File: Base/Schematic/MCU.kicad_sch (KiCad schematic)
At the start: 6 parts, among them U1 STM32F446RET6, X1 1532H4-12000JWPDTSNL

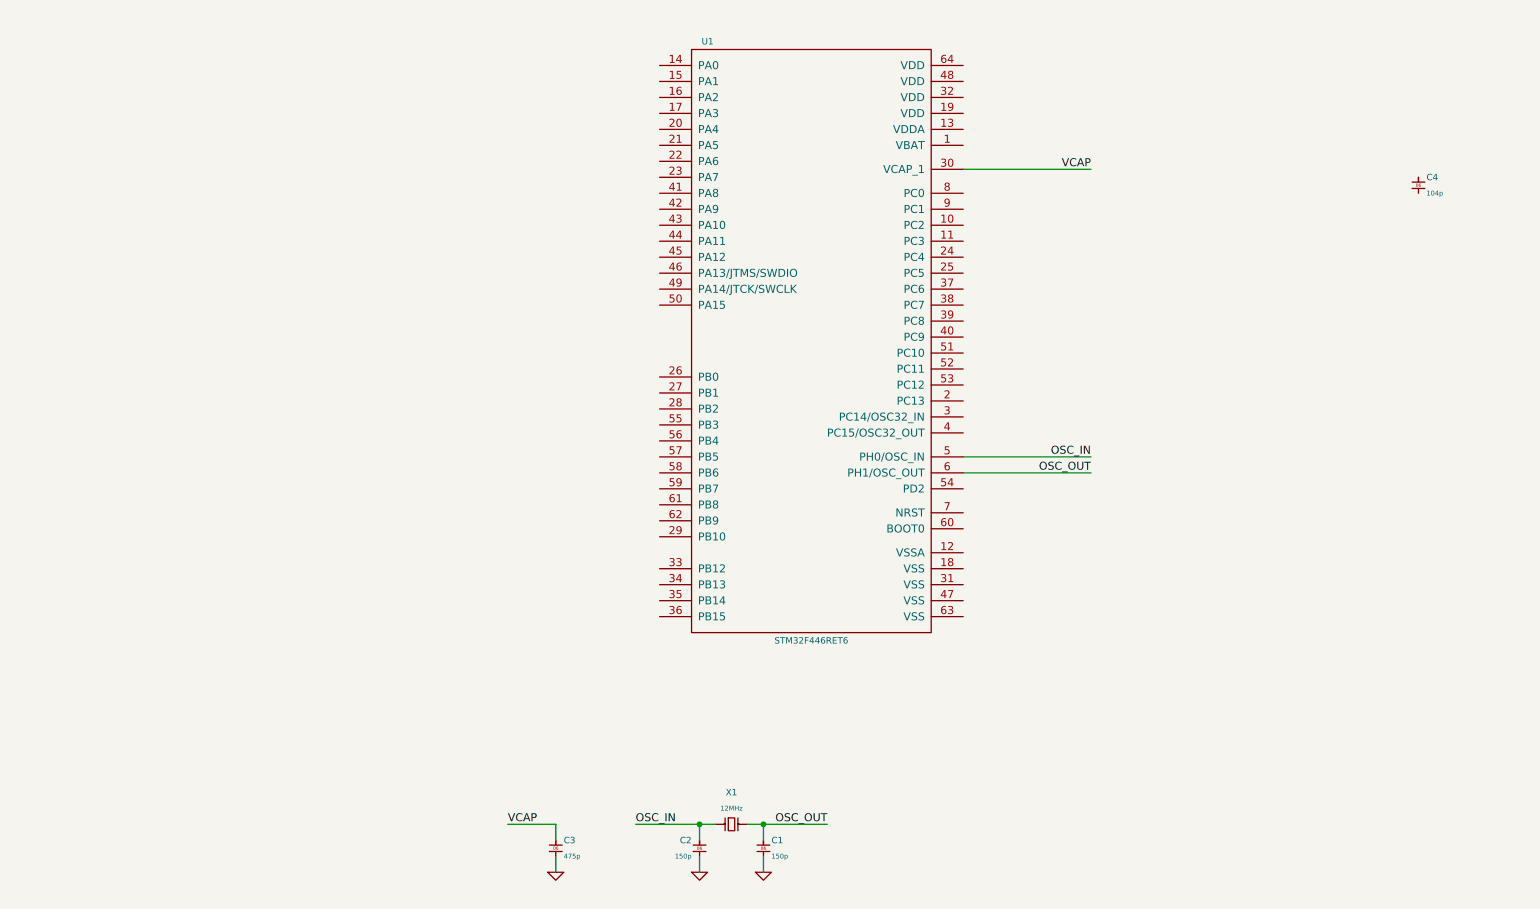
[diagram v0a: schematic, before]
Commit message: [Base 회로 업데이트] - 전원 회로 추가
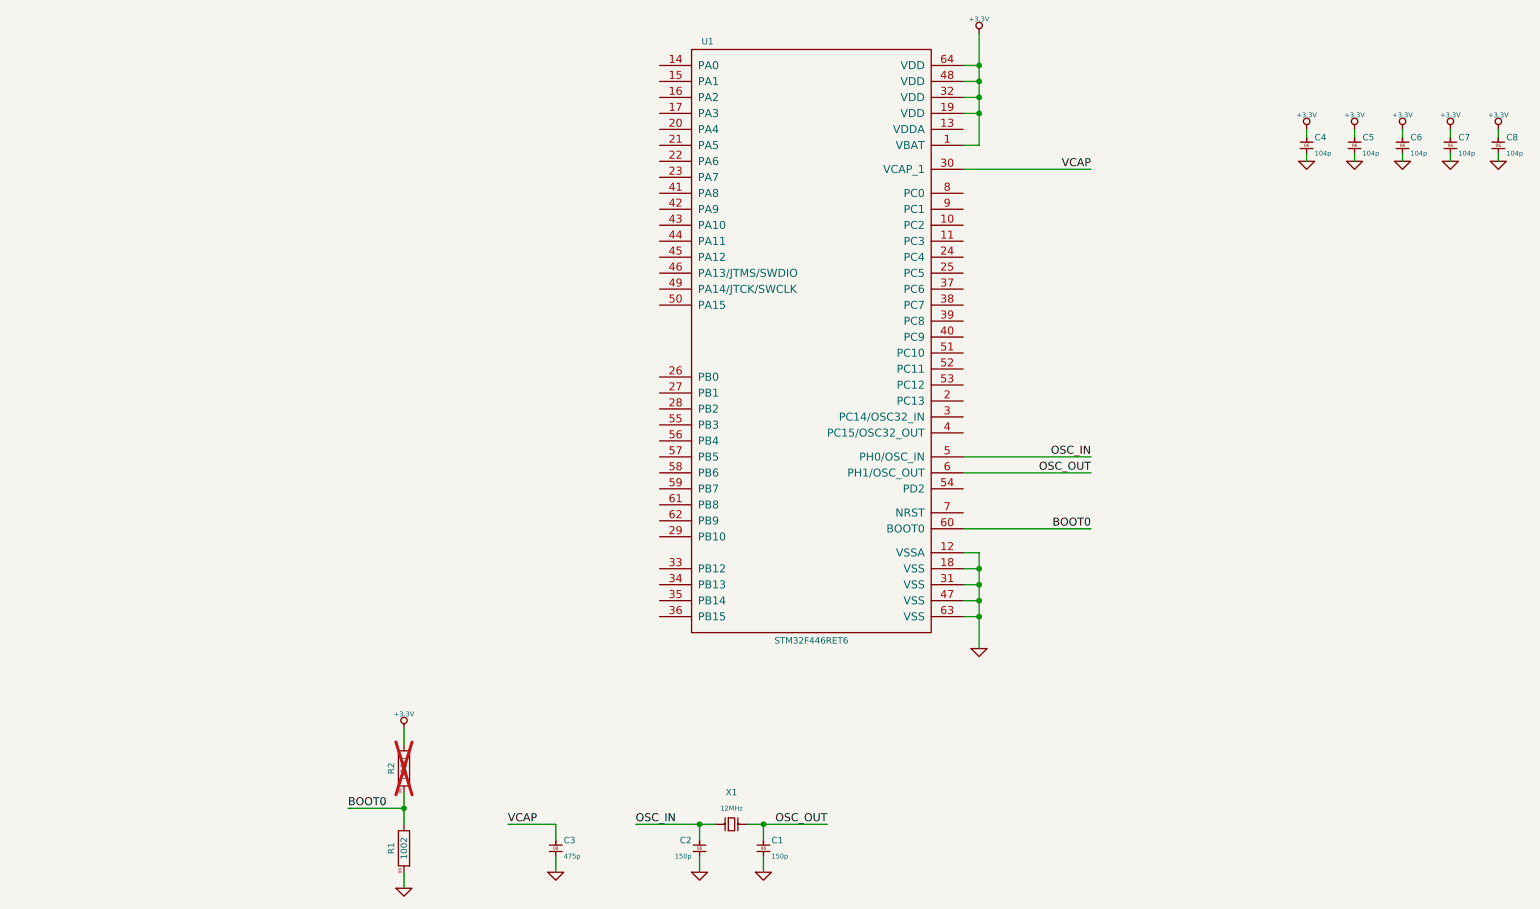
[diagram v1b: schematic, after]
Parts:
- added C5, C6, C7, C8: 0603B104K500, SMC:0603, symbol Capacitor_MLCC:0603B104K500
- added R1: WR06X1002FTL, SMR:0603, symbol Resistor:WR06X1002FTL
- added R2: WR06X0000JTL, SMR:0603, symbol Resistor:WR06X0000JTL
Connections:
- net GND: now also C4.1, U1.12 (VSSA), U1.18 (VSS), U1.31 (VSS), U1.47 (VSS), U1.63 (VSS), C5.1, C6.1, C7.1, C8.1, R1.1
- net +3.3V: now reaches U1.1 (VBAT)
- net +3.3V: now also C4.2, U1.19 (VDD), U1.32 (VDD), U1.48 (VDD), U1.64 (VDD), C5.2, C6.2, C7.2, C8.2, R2.2
- net BOOT0: now reaches U1.60 (BOOT0)
- net BOOT0: now also R1.2, R2.1
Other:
- moved on the sheet: C4

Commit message: [Base 회로도 업데이트] - MCU를 STM32F446 -> Nuvoton M433으로 변경
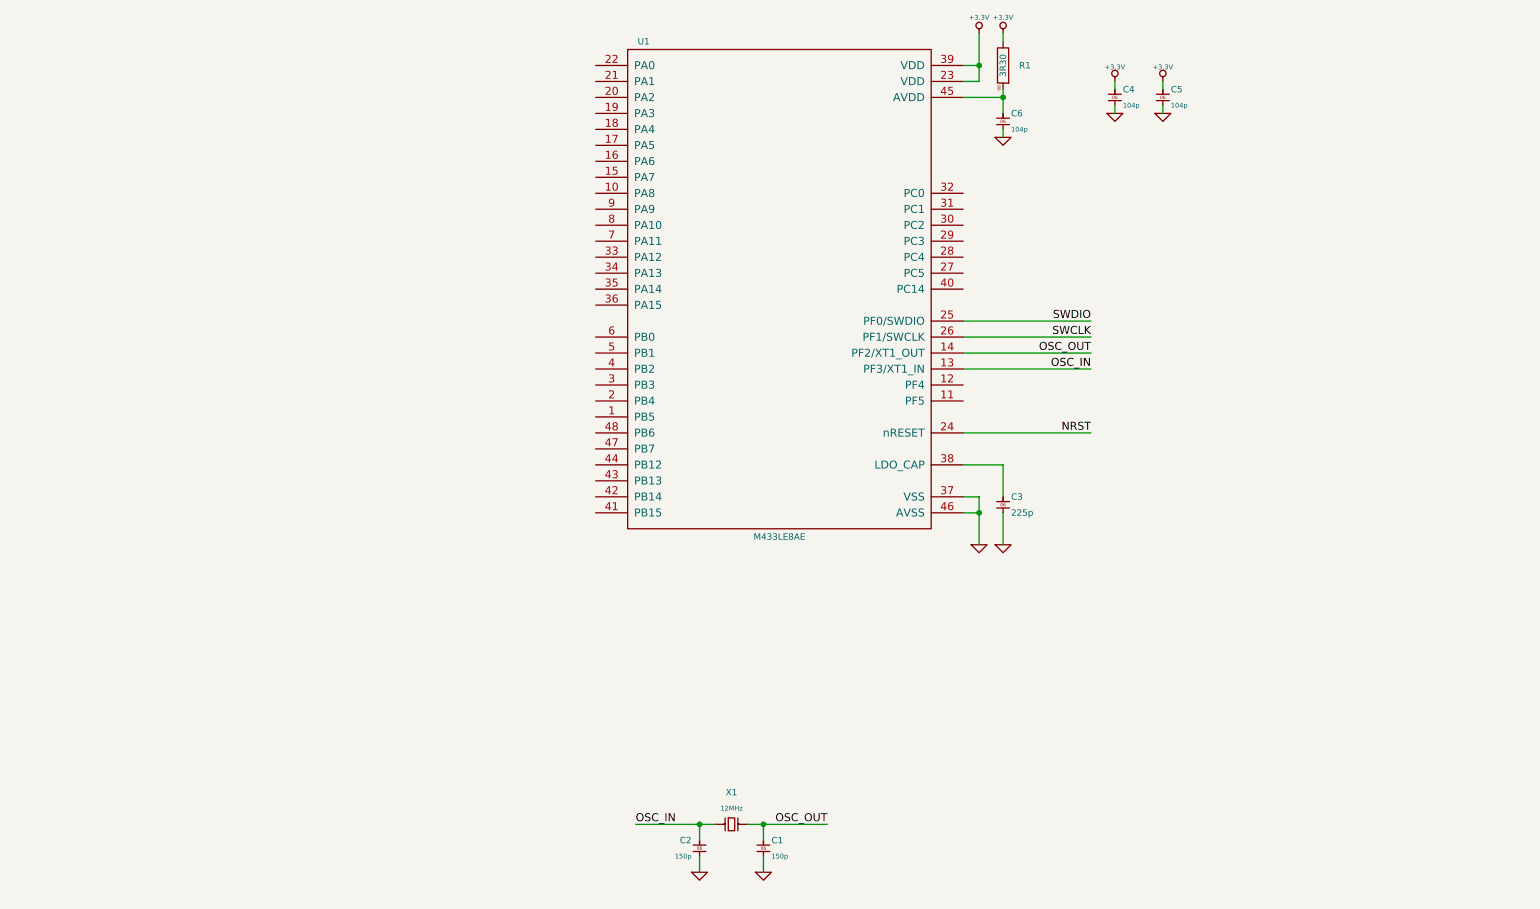
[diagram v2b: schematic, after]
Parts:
- removed C3: 0603X475K100, SMC:0603, symbol Capacitor_MLCC:0603X475K100
- removed C7, C8: 0603B104K500, SMC:0603, symbol Capacitor_MLCC:0603B104K500
- removed R1: WR06X1002FTL, SMR:0603, symbol Resistor:WR06X1002FTL
- removed R2: WR06X0000JTL, SMR:0603, symbol Resistor:WR06X0000JTL
- removed U1: STM32F446RET6, LQFP:LQFP64, symbol MCU:STM32F446RET6
- added C3: 0603X225K100, Capacitor_SMD:C_0603_1608Metric_Pad1.08x0.95mm_HandSolder, symbol Capacitor_MLCC:0603X225K100
- added R1: WR06W3R30FTL, SMR:0603, symbol Resistor:WR06W3R30FTL
- added U1: M433LE8AE, LQFP:LQFP48, symbol MCU:M433LE8AE
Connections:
- net +3.3V: now also R1.2, U1.23 (VDD), U1.39 (VDD); no longer C6.2
- net GND: now also C3.1, U1.37 (VSS), U1.46 (AVSS)
- net OSC_IN: now also U1.13 (PF3/XT1_IN)
- net OSC_OUT: now also U1.14 (PF2/XT1_OUT)
- new net: C6.2, R1.1, U1.45 (AVDD)
- new net: C3.2, U1.38 (LDO_CAP)
- new net NRST: U1.24 (nRESET)
- new net SWCLK: U1.26 (PF1/SWCLK)
- new net SWDIO: U1.25 (PF0/SWDIO)
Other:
- moved on the sheet: C4, C5

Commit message: [Base 회로도 업데이트] - RTC 회로 추가 - M433에는 VBAT 단자가 없어서 별도 부품으로 추가함
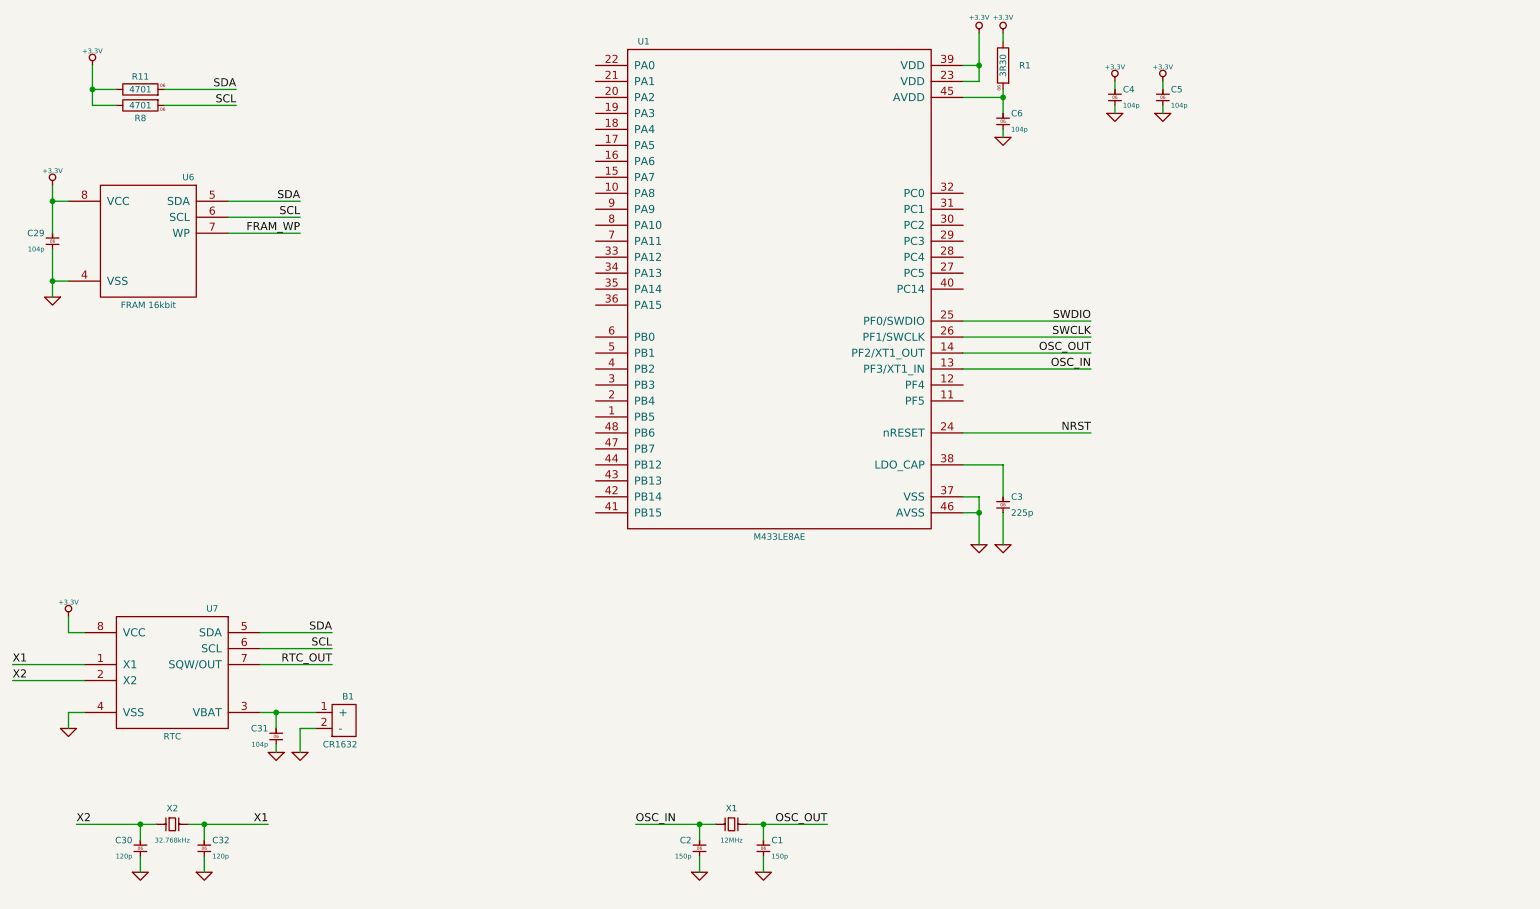
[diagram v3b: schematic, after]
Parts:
- added B1: GT-CR1632-1Au, G-Switch:GT-CR1632-1Au, symbol BatteryHolder:GT-CR1632-1Au
- added C29, C31: 0603B104K500, SMC:0603, symbol Capacitor_MLCC:0603B104K500
- added C30, C32: 0603N120J500, SMC:0603, symbol Capacitor_MLCC:0603N120J500
- added R11, R8: WR06X4701FTL, SMR:0603, symbol Resistor:WR06X4701FTL
- added U6: MB85RC16PNF-G-JNE, SO:SOIC-8, symbol FRAM:MB85RC16PNF-G-JNE
- added U7: SL1307ZN+T, SO:SOIC-8, symbol RTC:SL1307ZN+T
- added X2: XKXGI-SUA-32.768K, CRYSTAL:SMD_3215_2Pin, symbol Crystal:XKXGI-SUA-32.768K
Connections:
- net +3.3V: now also C29.2, R11.2, R8.2, U6.8 (VCC), U7.8 (VCC)
- net GND: now also B1.2 (-), C29.1, C30.1, C31.1, C32.1, U6.4 (VSS), U7.4 (VSS)
- new net: B1.1 (+), C31.2, U7.3 (VBAT)
- new net FRAM_WP: U6.7 (WP)
- new net RTC_OUT: U7.7 (SQW/OUT)
- new net SCL: R8.1, U6.6 (SCL), U7.6 (SCL)
- new net SDA: R11.1, U6.5 (SDA), U7.5 (SDA)
- new net X1: C32.2, U7.1 (X1), X2.2
- new net X2: C30.2, U7.2 (X2), X2.1

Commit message: [Base PCB 업데이트] - PCB 외곽선과 볼트 위치 설정
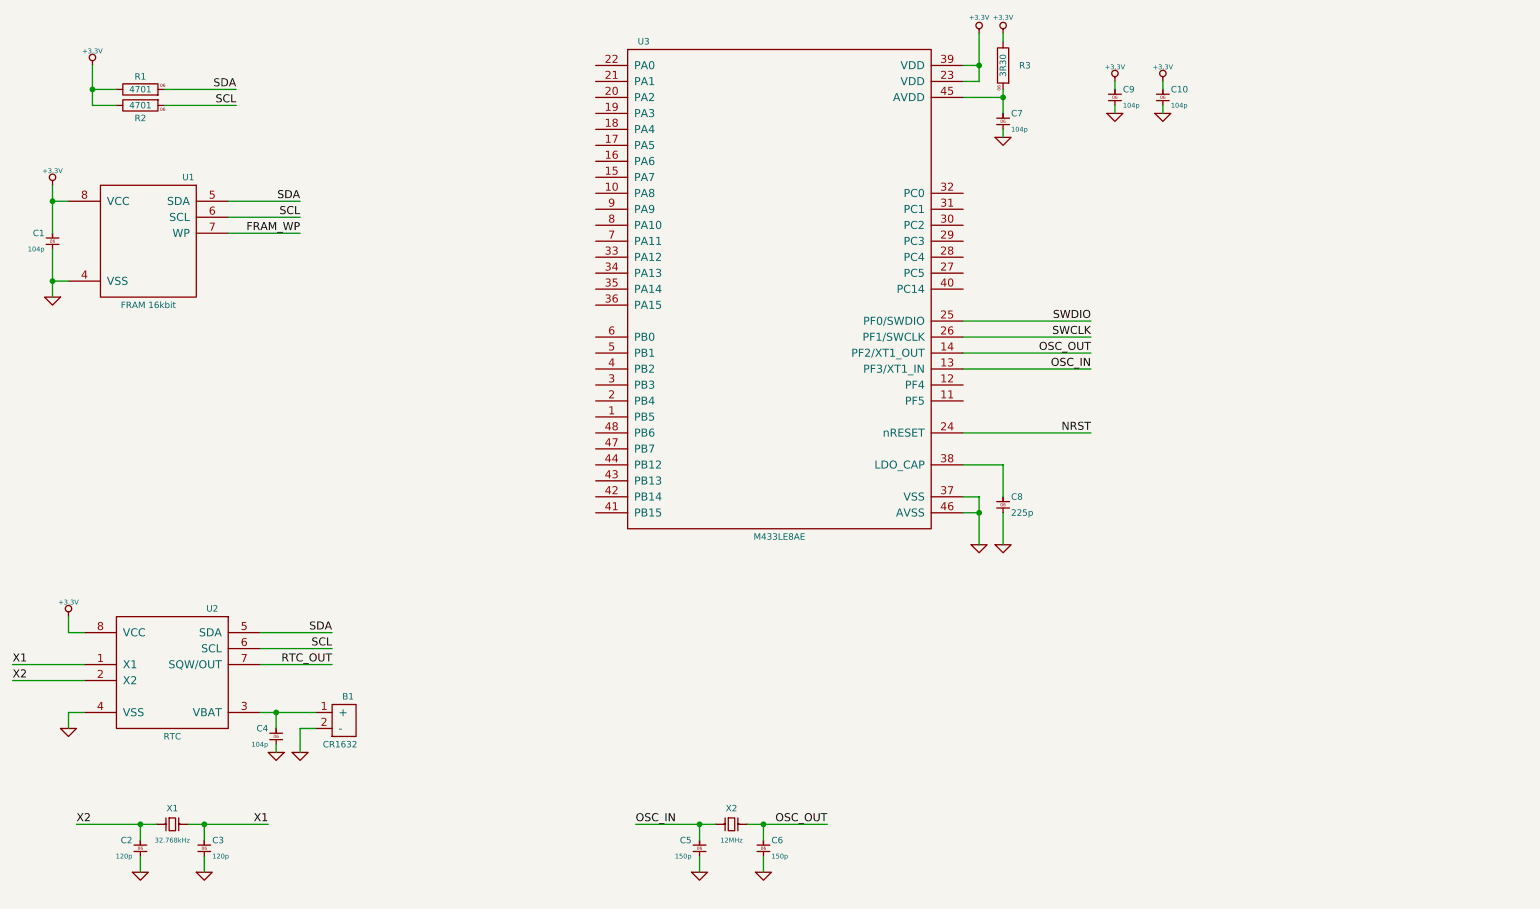
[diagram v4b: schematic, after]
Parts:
- renumbered C29 to C1, C5 to C10, C30 to C2, C32 to C3, C31 to C4, C2 to C5, C1 to C6, C6 to C7, C3 to C8, C4 to C9, R11 to R1, R8 to R2, R1 to R3, U6 to U1, U7 to U2, U1 to U3, X2 to X1, X1 to X2
